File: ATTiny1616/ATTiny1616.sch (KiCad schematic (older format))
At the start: 22 parts, among them J1 Conn_01x10, J2 Conn_01x02, J3 Conn_01x10, J4 ISP6, SW1 RST, U1 AP2204K-ADJ, U2 ATtiny3216-M

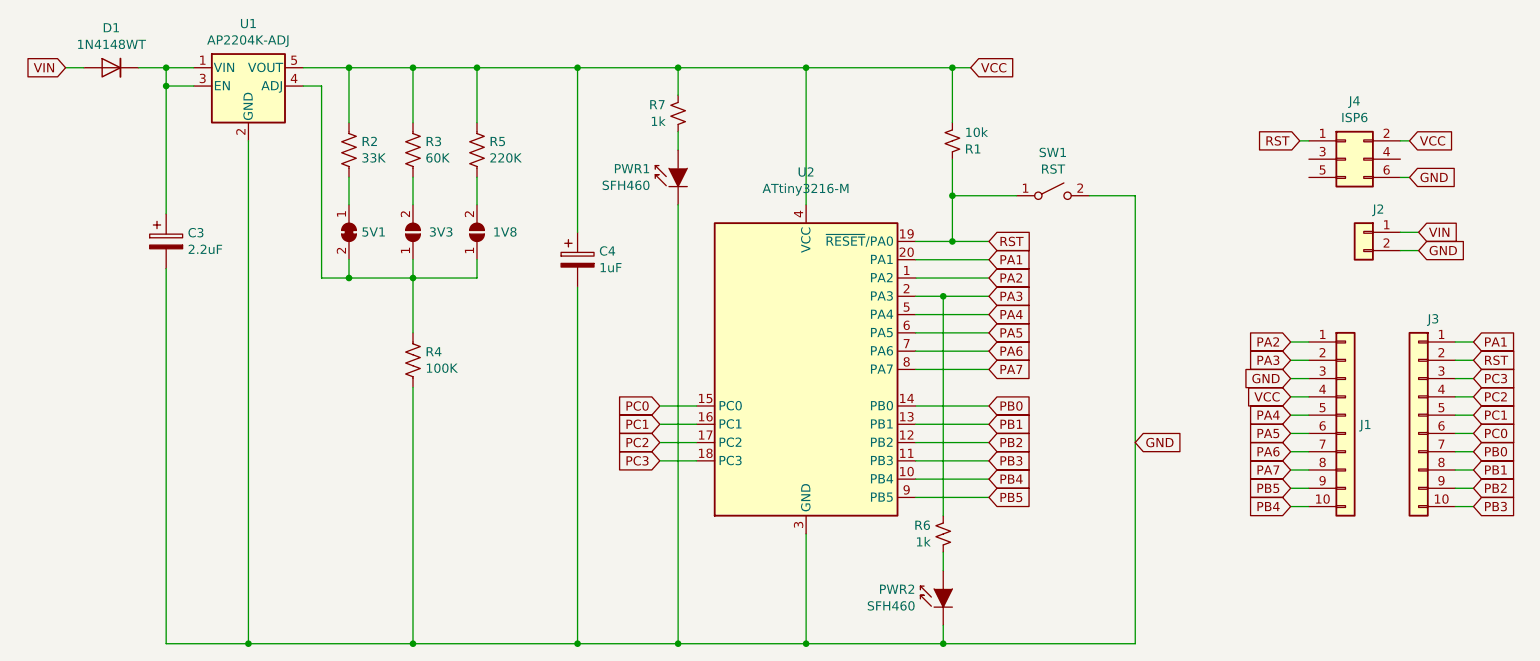
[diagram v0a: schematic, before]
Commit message: Silkscreens Orientated
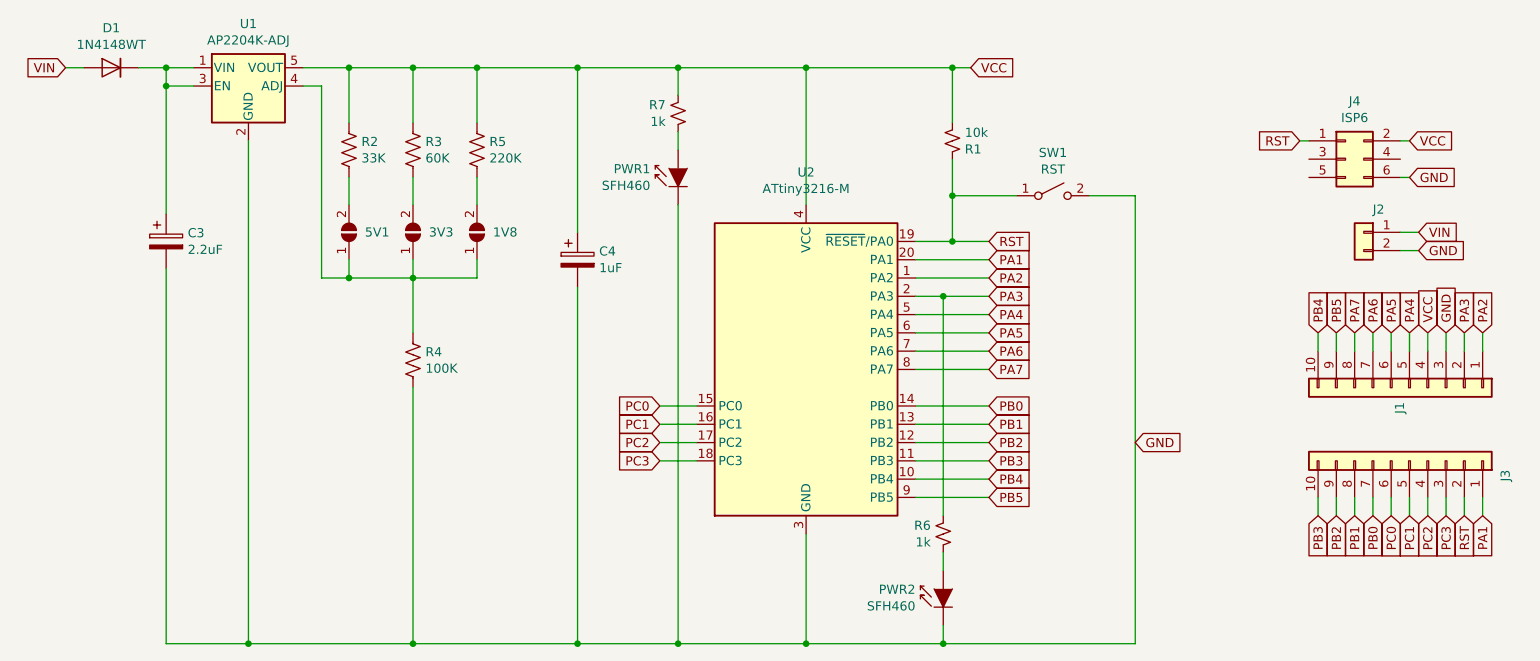
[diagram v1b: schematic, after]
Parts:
- removed 5V1: SolderJumper_2_Bridged, Jumper:SolderJumper-2_P1.3mm_Bridged_RoundedPad1.0x1.5mm, symbol Jumper:SolderJumper_2_Bridged
- added 5V1: SolderJumper_2_Open, Jumper:SolderJumper-2_P1.3mm_Open_RoundedPad1.0x1.5mm, symbol Jumper:SolderJumper_2_Open
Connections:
- net at R2.2: now also 5V1.2 (B)
- net at 1V8.1 (A), 3V3.1 (A), R4.1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: now also 5V1.1 (A)
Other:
- moved on the sheet: J1, J3
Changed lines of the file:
@@
 	3550 2850 3700 2850
 Wire Wire Line
-	10600 4450 10700 4450
+	10650 5200 10650 5300
 Text GLabel 8050 4100 2    50   Input ~ 0
 PA3
@@
 Wire Wire Line
 	6350 3000 6350 2850
-Text GLabel 10700 4450 2    50   Input ~ 0
+Text GLabel 10650 5300 3    50   Input ~ 0
 RST
 Connection ~ 6350 2850
@@
 Wire Wire Line
 	4300 2950 4400 2950
-$Comp
-L Jumper:SolderJumper_2_Bridged 5V1
-U 1 1 5D4D08FE
-P 4550 3750
-F 0 "5V1" V 4550 3818 50  0000 L CNN
-F 1 "SolderJumper_2_Bridged" V 4595 3818 50  0001 L CNN
-F 2 "Jumper:SolderJumper-2_P1.3mm_Bridged_RoundedPad1.0x1.5mm" H 4550 3750 50  0001 C CNN
-F 3 "~" H 4550 3750 50  0001 C CNN
-	1    4550 3750
-	0    1    1    0
-$EndComp
 Wire Wire Line
 	5250 3450 5250 3600
@@
 	8050 4900 7650 4900
 Wire Wire Line
-	10700 4350 10600 4350
-Text GLabel 10700 4350 2    50   Input ~ 0
+	10750 5300 10750 5200
+Text GLabel 10750 5300 3    50   Input ~ 0
 PA1
 Wire Wire Line
-	9700 4850 9800 4850
-Wire Wire Line
-	9800 4750 9700 4750
-Text GLabel 9700 4750 0    50   Input ~ 0
+	10250 4300 10250 4400
+Wire Wire Line
+	10350 4400 10350 4300
+Text GLabel 10350 4300 1    50   Input ~ 0
 PA4
-Text GLabel 9700 4850 0    50   Input ~ 0
+Text GLabel 10250 4300 1    50   Input ~ 0
 PA5
 Wire Wire Line
-	9800 4950 9700 4950
-Wire Wire Line
-	9800 5050 9700 5050
-Text GLabel 9700 4950 0    50   Input ~ 0
+	10150 4400 10150 4300
+Wire Wire Line
+	10050 4400 10050 4300
+Text GLabel 10150 4300 1    50   Input ~ 0
 PA6
-Text GLabel 9700 5050 0    50   Input ~ 0
+Text GLabel 10050 4300 1    50   Input ~ 0
 PA7
 $Comp
@@
 L Connector_Generic:Conn_01x10 J1
 U 1 1 5D4C49C3
-P 10000 4750
-F 0 "J1" H 10079 4697 50  0000 L CNN
-F 1 "Conn_01x10" H 10079 4652 50  0001 L CNN
-F 2 "Connector_PinHeader_2.54mm:PinHeader_1x10_P2.54mm_Vertical" H 10000 4750 50  0001 C CNN
-F 3 "~" H 10000 4750 50  0001 C CNN
-	1    10000 4750
-	1    0    0    -1
+P 10350 4600
+F 0 "J1" H 10429 4547 50  0000 L CNN
+F 1 "Conn_01x10" H 10429 4502 50  0001 L CNN
+F 2 "Connector_PinHeader_2.54mm:PinHeader_1x10_P2.54mm_Vertical" H 10350 4600 50  0001 C CNN
+F 3 "~" H 10350 4600 50  0001 C CNN
+	1    10350 4600
+	0    1    1    0
 $EndComp
 $Comp
 L Connector_Generic:Conn_01x10 J3
 U 1 1 5D4C752A
-P 10400 4750
-F 0 "J3" H 10319 5275 50  0000 C CNN
-F 1 "Conn_01x10" H 10479 4652 50  0001 L CNN
-F 2 "Connector_PinHeader_2.54mm:PinHeader_1x10_P2.54mm_Vertical" H 10400 4750 50  0001 C CNN
-F 3 "~" H 10400 4750 50  0001 C CNN
-	1    10400 4750
-	-1   0    0    -1
-$EndComp
-Wire Wire Line
-	9700 4350 9800 4350
-Text GLabel 9700 4350 0    50   Input ~ 0
+P 10350 5000
+F 0 "J3" H 10269 5525 50  0000 C CNN
+F 1 "Conn_01x10" H 10429 4902 50  0001 L CNN
+F 2 "Connector_PinHeader_2.54mm:PinHeader_1x10_P2.54mm_Vertical" H 10350 5000 50  0001 C CNN
+F 3 "~" H 10350 5000 50  0001 C CNN
+	1    10350 5000
+	0    1    -1   0
+$EndComp
+Wire Wire Line
+	10750 4300 10750 4400
+Text GLabel 10750 4300 1    50   Input ~ 0
 PA2
 Wire Wire Line
-	9700 4450 9800 4450
-Text GLabel 9700 4450 0    50   Input ~ 0
+	10650 4300 10650 4400
+Text GLabel 10650 4300 1    50   Input ~ 0
 PA3
-Text GLabel 9700 4550 0    50   Input ~ 0
+Text GLabel 10550 4300 1    50   Input ~ 0
 GND
 Wire Wire Line
-	9800 4550 9700 4550
-Text GLabel 9700 4650 0    50   Input ~ 0
+	10550 4400 10550 4300
+Text GLabel 10450 4300 1    50   Input ~ 0
 VCC
 Wire Wire Line
-	9800 4650 9700 4650
-Text GLabel 9700 5250 0    50   Input ~ 0
+	10450 4400 10450 4300
+Text GLabel 9850 4300 1    50   Input ~ 0
 PB4
-Text GLabel 9700 5150 0    50   Input ~ 0
+Text GLabel 9950 4300 1    50   Input ~ 0
 PB5
 Wire Wire Line
-	9700 5250 9800 5250
-Wire Wire Line
-	9800 5150 9700 5150
-Wire Wire Line
-	10600 5250 10700 5250
-Wire Wire Line
-	10700 5150 10600 5150
-Text GLabel 10700 5250 2    50   Input ~ 0
+	9850 4300 9850 4400
+Wire Wire Line
+	9950 4400 9950 4300
+Wire Wire Line
+	9850 5200 9850 5300
+Wire Wire Line
+	9950 5300 9950 5200
+Text GLabel 9850 5300 3    50   Input ~ 0
 PB3
-Text GLabel 10700 5150 2    50   Input ~ 0
+Text GLabel 9950 5300 3    50   Input ~ 0
 PB2
-Text GLabel 10700 5050 2    50   Input ~ 0
+Text GLabel 10050 5300 3    50   Input ~ 0
 PB1
-Text GLabel 10700 4950 2    50   Input ~ 0
+Text GLabel 10150 5300 3    50   Input ~ 0
 PB0
 Wire Wire Line
-	10700 4950 10600 4950
-Wire Wire Line
-	10600 5050 10700 5050
-Text GLabel 10700 4650 2    50   Input ~ 0
+	10150 5300 10150 5200
+Wire Wire Line
+	10050 5200 10050 5300
+Text GLabel 10450 5300 3    50   Input ~ 0
 PC2
-Text GLabel 10700 4750 2    50   Input ~ 0
+Text GLabel 10350 5300 3    50   Input ~ 0
 PC1
-Text GLabel 10700 4550 2    50   Input ~ 0
+Text GLabel 10550 5300 3    50   Input ~ 0
 PC3
-Text GLabel 10700 4850 2    50   Input ~ 0
+Text GLabel 10250 5300 3    50   Input ~ 0
 PC0
 Wire Wire Line
-	10700 4850 10600 4850
-Wire Wire Line
-	10700 4650 10600 4650
-Wire Wire Line
-	10600 4750 10700 4750
-Wire Wire Line
-	10600 4550 10700 4550
+	10250 5300 10250 5200
+Wire Wire Line
+	10450 5300 10450 5200
+Wire Wire Line
+	10350 5200 10350 5300
+Wire Wire Line
+	10550 5200 10550 5300
 Connection ~ 7800 4100
 Wire Wire Line
@@
 Wire Wire Line
 	7650 5000 8050 5000
+$Comp
+L Jumper:SolderJumper_2_Open 5V1
+U 1 1 5D5DACE6
+P 4550 3750
+F 0 "5V1" V 4550 3663 50  0000 R CNN
+F 1 "SolderJumper_2_Open" H 4550 3863 50  0001 C CNN
+F 2 "Jumper:SolderJumper-2_P1.3mm_Open_RoundedPad1.0x1.5mm" H 4550 3750 50  0001 C CNN
+F 3 "~" H 4550 3750 50  0001 C CNN
+	1    4550 3750
+	0    -1   -1   0
+$EndComp
 $EndSCHEMATC
